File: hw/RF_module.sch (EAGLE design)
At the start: 27 parts, among them J1 R2P_BUS-VERTICAL, J2 R2P_BUS-VERTICAL

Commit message: Updated keepout
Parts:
- C1: device r2p_rcl:C-1206 -> r2p_rcl:C1206
- C14, C17, C2, C3, C4, C6, C7, C8: device r2p_rcl:C-0603 -> r2p_rcl:C0603
- C5, C9: device r2p_rcl:C-0805 -> r2p_rcl:C0805
- R1, R2: device r2p_rcl:R-0603 -> r2p_rcl:R0603
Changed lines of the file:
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@@
 </classes>
 <parts>
-<part name="C6" library="r2p_rcl" deviceset="C" device="-0603" value="10n"/>
+<part name="C6" library="r2p_rcl" deviceset="C" device="0603" value="10n"/>
 <part name="GND11" library="r2p_supply" deviceset="GND" device=""/>
 <part name="GND12" library="r2p_supply" deviceset="GND" device=""/>
@@
 <part name="GND6" library="r2p_supply" deviceset="GND" device=""/>
 <part name="+3V4" library="r2p_supply" deviceset="+3V3" device=""/>
-<part name="C17" library="r2p_rcl" deviceset="C" device="-0603" value="100n"/>
-<part name="C14" library="r2p_rcl" deviceset="C" device="-0603" value="100n"/>
-<part name="C4" library="r2p_rcl" deviceset="C" device="-0603" value="100n"/>
+<part name="C17" library="r2p_rcl" deviceset="C" device="0603" value="100n"/>
+<part name="C14" library="r2p_rcl" deviceset="C" device="0603" value="100n"/>
+<part name="C4" library="r2p_rcl" deviceset="C" device="0603" value="100n"/>
 <part name="GND29" library="r2p_supply" deviceset="GND" device=""/>
 <part name="GND30" library="r2p_supply" deviceset="GND" device=""/>
 <part name="GND31" library="r2p_supply" deviceset="GND" device=""/>
 <part name="+3V11" library="r2p_supply" deviceset="+3V3" device=""/>
-<part name="C5" library="r2p_rcl" deviceset="C" device="-0805" value="4.7u"/>
+<part name="C5" library="r2p_rcl" deviceset="C" device="0805" value="4.7u"/>
 <part name="GND34" library="r2p_supply" deviceset="GND" device=""/>
 <part name="+3V5" library="r2p_supply" deviceset="+3V3" device=""/>
 <part name="GND7" library="r2p_supply" deviceset="GND" device=""/>
 <part name="+3V6" library="r2p_supply" deviceset="+3V3" device=""/>
-<part name="C3" library="r2p_rcl" deviceset="C" device="-0603" value="100n"/>
+<part name="C3" library="r2p_rcl" deviceset="C" device="0603" value="100n"/>
 <part name="GND9" library="r2p_supply" deviceset="GND" device=""/>
 <part name="+3V3" library="r2p_supply" deviceset="+3V3" device=""/>
 <part name="GND8" library="r2p_supply" deviceset="GND" device=""/>
 <part name="GND10" library="r2p_supply" deviceset="GND" device=""/>
-<part name="C7" library="r2p_rcl" deviceset="C" device="-0603" value="100n"/>
+<part name="C7" library="r2p_rcl" deviceset="C" device="0603" value="100n"/>
 <part name="GND22" library="r2p_supply" deviceset="GND" device=""/>
 <part name="LED1" library="r2p_led" deviceset="LED" device="0805" value=""/>
-<part name="R1" library="r2p_rcl" deviceset="R" device="-0603" value="330"/>
+<part name="R1" library="r2p_rcl" deviceset="R" device="0603" value="330"/>
 <part name="GND16" library="r2p_supply" deviceset="GND" device=""/>
 <part name="GND17" library="r2p_supply" deviceset="GND" device=""/>
@@
 <part name="J2" library="r2p_connector" deviceset="R2P_BUS" device="-VERTICAL"/>
 <part name="U$2" library="r2p_rcl" deviceset="LPS4018" device=""/>
-<part name="C1" library="r2p_rcl" deviceset="C" device="-1206" value="1u"/>
+<part name="C1" library="r2p_rcl" deviceset="C" device="1206" value="1u"/>
 <part name="GND1" library="r2p_supply" deviceset="GND" device=""/>
-<part name="C2" library="r2p_rcl" deviceset="C" device="-0603" value="1u"/>
-<part name="C8" library="r2p_rcl" deviceset="C" device="-0603" value="10n"/>
+<part name="C2" library="r2p_rcl" deviceset="C" device="0603" value="1u"/>
+<part name="C8" library="r2p_rcl" deviceset="C" device="0603" value="10n"/>
 <part name="GND4" library="r2p_supply" deviceset="GND" device=""/>
 <part name="GND5" library="r2p_supply" deviceset="GND" device=""/>
-<part name="C9" library="r2p_rcl" deviceset="C" device="-0805" value="10u"/>
+<part name="C9" library="r2p_rcl" deviceset="C" device="0805" value="10u"/>
 <part name="GND2" library="r2p_supply" deviceset="GND" device=""/>
 <part name="GND3" library="r2p_supply" deviceset="GND" device=""/>
@@
 <part name="GND20" library="r2p_supply" deviceset="GND" device=""/>
 <part name="GND21" library="r2p_supply" deviceset="GND" device=""/>
-<part name="R2" library="r2p_rcl" deviceset="R" device="-0603" value="330"/>
+<part name="R2" library="r2p_rcl" deviceset="R" device="0603" value="330"/>
 </parts>
 <sheets>

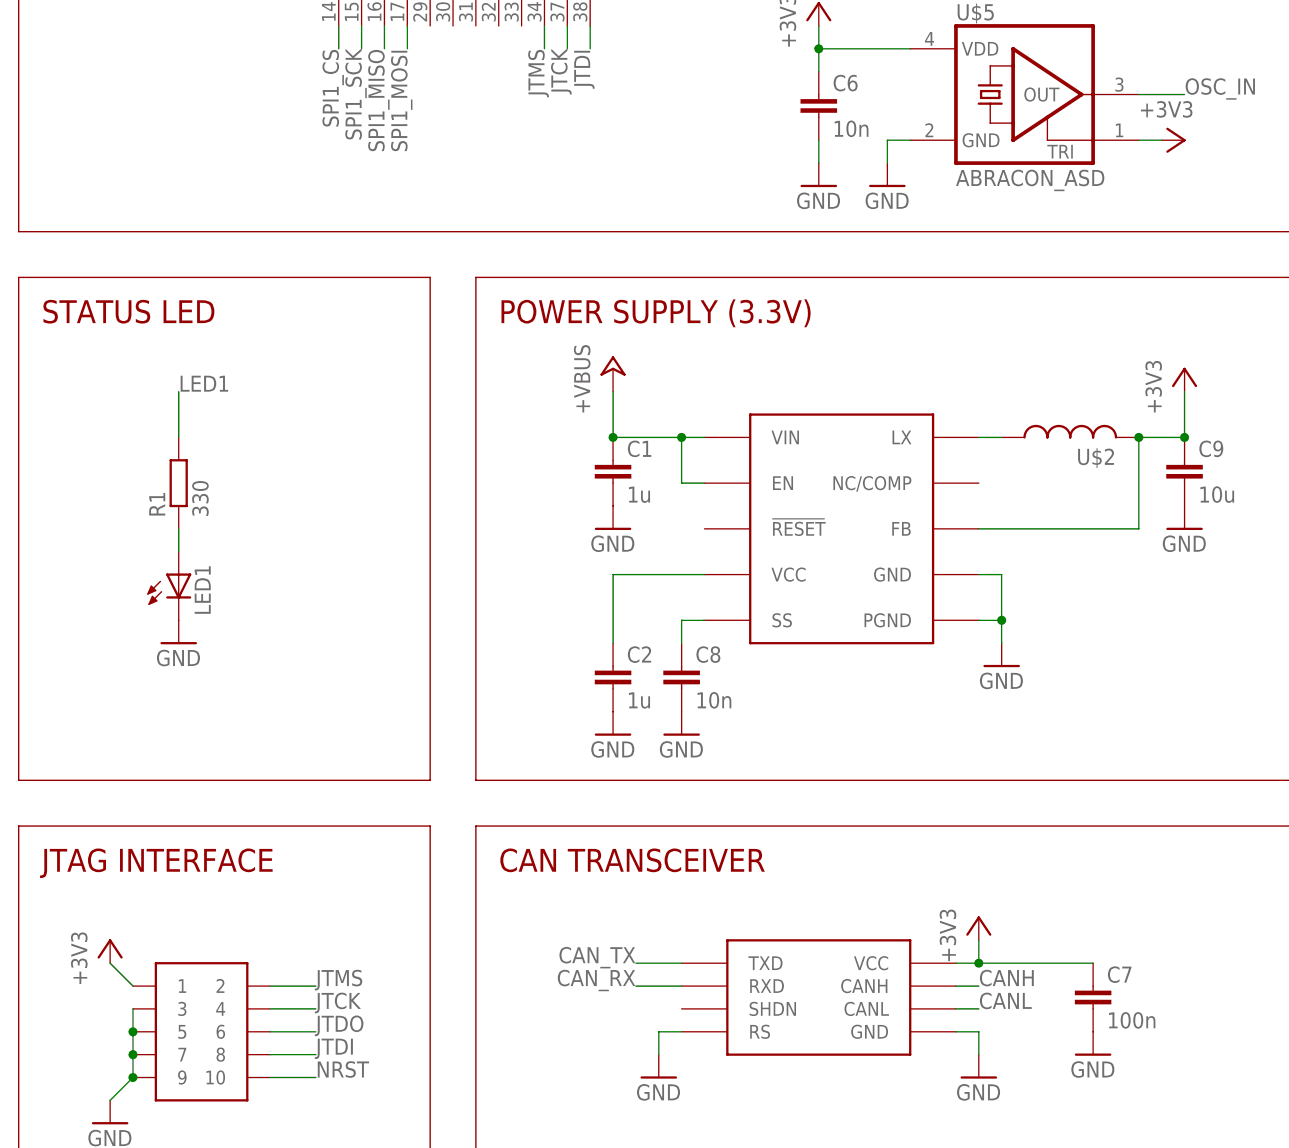
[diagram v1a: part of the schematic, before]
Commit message: Fixed silkscreen
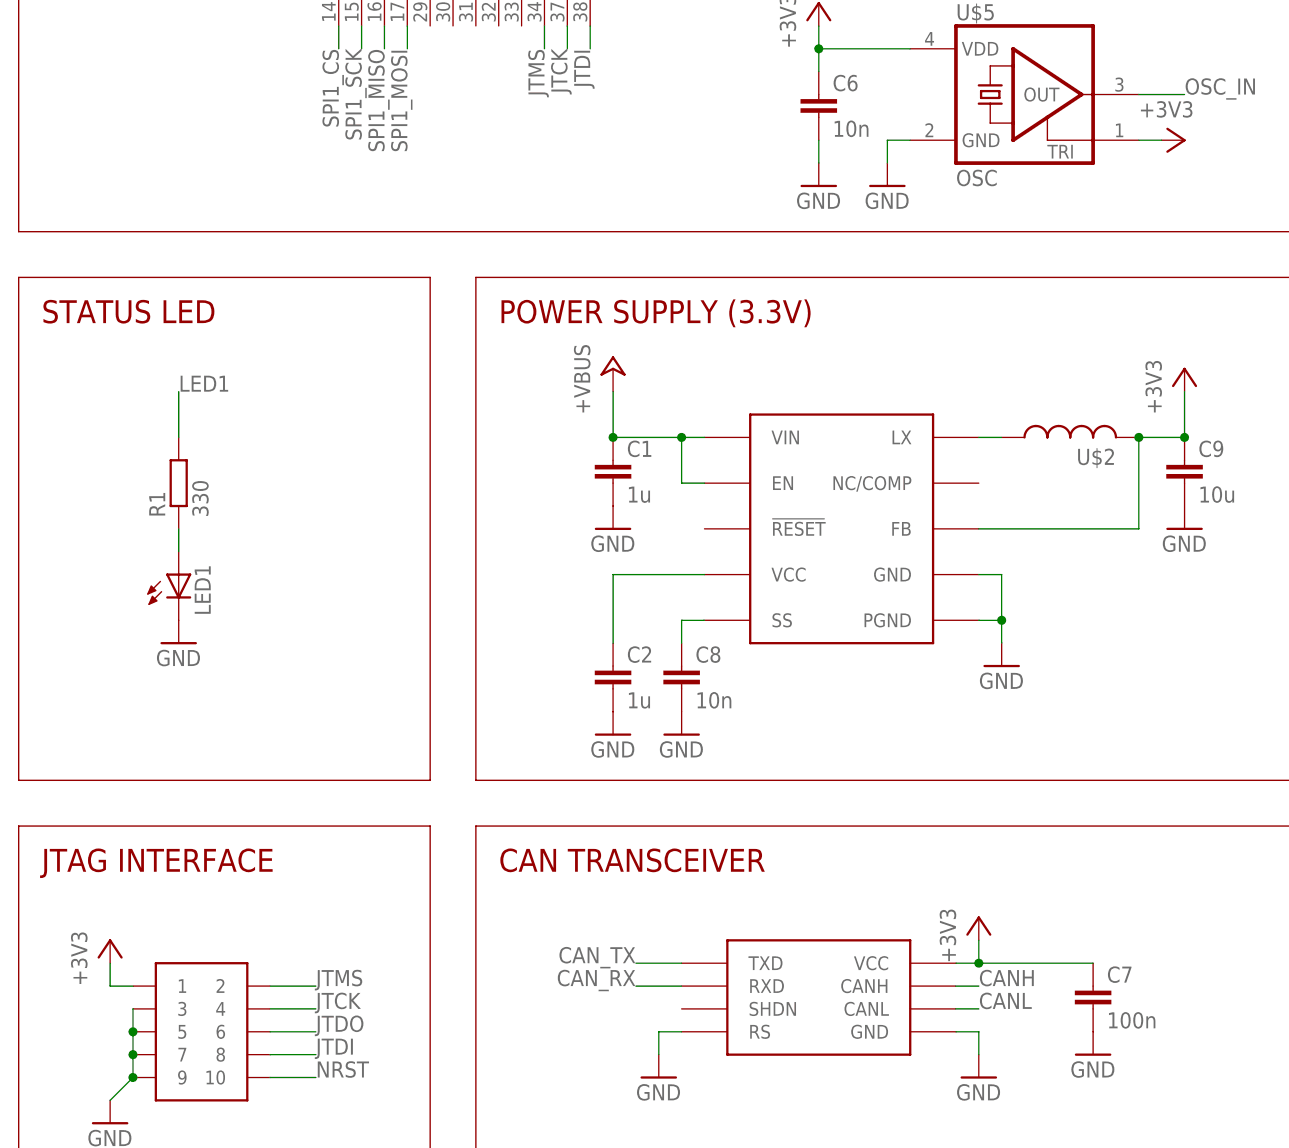
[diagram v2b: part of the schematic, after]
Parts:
- U$5: value ABRACON_ASD -> OSC; device r2p_ic:ABRACON_ASD -> r2p_ic:OSC
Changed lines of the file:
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@@
 <part name="SOT1" library="r2p_ic" deviceset="MAX3051" device="EKA"/>
 <part name="U$1" library="r2p_pcb" deviceset="PCB_25X45" device=""/>
-<part name="U$5" library="r2p_ic" deviceset="ABRACON_ASD" device=""/>
+<part name="U$5" library="r2p_ic" deviceset="OSC" device=""/>
 <part name="+3V7" library="r2p_supply" deviceset="+3V3" device=""/>
 <part name="U$7" library="r2p_supply" deviceset="+VBUS" device=""/>
@@
 </segment>
 <segment>
-<wire x1="17.78" y1="71.12" x2="15.24" y2="73.66" width="0.1524" layer="91"/>
+<wire x1="17.78" y1="71.12" x2="15.24" y2="71.12" width="0.1524" layer="91"/>
+<wire x1="15.24" y1="71.12" x2="15.24" y2="73.66" width="0.1524" layer="91"/>
 <pinref part="U$4" gate="G$1" pin="1"/>
 <pinref part="+3V1" gate="G$1" pin="+3V3"/>
